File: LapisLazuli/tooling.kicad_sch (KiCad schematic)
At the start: 60 parts, among them J1 Conn_01x02, J10 Conn_01x03, J11 Conn_01x03, J12 Conn_01x02, J13 Conn_01x02, J2 Conn_01x02, J3 Conn_01x02, J4 Conn_01x02, J5 Conn_01x02, J6 Conn_01x02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

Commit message: Everything but I2C mux I think
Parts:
- added C44: 100n, symbol Device:C_Small
- added C45: 10u, symbol Device:C_Small
- added J14, J15: Conn_01x04, symbol Connector_Generic:Conn_01x04
- added J16: Conn_01x02, symbol Connector_Generic:Conn_01x02
- added R21: 120, symbol Device:R_Small_US
- added U13: LTC4311CSC6-TRPBF, SOT-6_SC_LIT, symbol 2025-11-21_17-52-57:LTC4311CSC6-TRPBF
- added U9: ISO1412DW, DW16_TEX, symbol 2025-11-15_19-07-41:ISO1412DW
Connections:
- net +5V: now also C44.2, C45.1, J14.4 (Pin_4), J15.4 (Pin_4), U13.1 (VCC), U13.3 (ENABLE), U9.1 (VCC1)
- net GND: now also C44.1, C45.2, J14.1 (Pin_1), J15.1 (Pin_1), U13.2 (GND), U13.5 (GND), U9.2 (GND1), U9.8 (GND1)
- net I2C_SCL: now also U13.4 (BUS2)
- net I2C_SDA: now also U13.6 (BUS1)
- new net ENCODER0_SCL: J14.2 (Pin_2)
- new net ENCODER0_SDA: J14.3 (Pin_3)
- new net ENCODER1_SCL: J15.2 (Pin_2)
- new net ENCODER1_SDA: J15.3 (Pin_3)
- new net GNDPWR: U9.15 (GND2), U9.9 (GND2)
- new net RS485_A: J16.2 (Pin_2), R21.1, U9.14 (A)
- new net RS485_B: J16.1 (Pin_1), R21.2, U9.13 (B)
- new net RS485_RX: U9.3 (R)
- new net RS485_SEND: U9.4 (*RE), U9.5 (DE)
- new net RS485_TX: U9.6 (D)
- no-connect marks 0 -> 2
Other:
- note added: "Encoder Headers"
- note added: "I2C Extender"
- note added: "RS485"
- note added: "idk what to do here"

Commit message: I2C Mux
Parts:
- added C46: 100n, symbol Device:C_Small
- added R22: 10k, symbol Device:R_Small_US
- added U14: TCA9546APWR, TCA9546APWR:SOP65P640X120-16N, symbol TCA9546APWR:TCA9546APWR
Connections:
- net +5V: now also C46.1, U14.16 (VCC)
- net ENCODER0_SCL: now also U14.5 (SC0)
- net ENCODER0_SDA: now also U14.4 (SD0)
- net ENCODER1_SCL: now also U14.7 (SC1)
- net ENCODER1_SDA: now also U14.6 (SD1)
- net GND: now also C46.2, U14.1 (A0), U14.13 (A2), U14.2 (A1), U14.8 (GND)
- net I2C_SCL: now also U14.15 (SDA)
- net I2C_SDA: now also U14.14 (SCL)
- new net I2C_MUX_RESET': R22.2, U14.3 (~{RESET})
- no-connect marks 2 -> 6
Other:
- note added: "I2C Mux"

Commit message: Most footprints and second I2C extender
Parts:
- added C47: 10u, Capacitor_SMD:C_0805_2012Metric, symbol Device:C_Small
- added U15: LTC4311CSC6-TRPBF, Package_TO_SOT_SMD:SOT-363_SC-70-6, symbol 2025-11-21_17-52-57:LTC4311CSC6-TRPBF
- C1, C10, C13, C14, C15, C16, C2, C35, C37, C39, C4, C41, C43, C44, C46, C5, C7, C8, C9: footprint (none) -> Capacitor_SMD:C_0603_1608Metric; Digikey (none) -> C14663; LCSC (none) -> C14663
- C11, C12, C3, C6: footprint (none) -> Capacitor_SMD:C_0805_2012Metric; Digikey (none) -> C16780; LCSC (none) -> C16780
- C36, C38, C40, C42: footprint (none) -> Capacitor_SMD:CP_Elec_6.3x7.7; Digikey (none) -> C3338; LCSC (none) -> C3338
- C45: footprint (none) -> Capacitor_SMD:C_0805_2012Metric; Digikey (none) -> C19702; LCSC (none) -> C19702
- J1, J12, J13, J16, J2, J3, J4, J5, J6: footprint (none) -> Connector_PinHeader_2.54mm:PinHeader_1x02_P2.54mm_Vertical
- J10, J11, J8, J9: footprint (none) -> Connector_PinHeader_2.54mm:PinHeader_1x03_P2.54mm_Vertical
- J14, J15: footprint (none) -> Connector_PinHeader_2.54mm:PinHeader_1x04_P2.54mm_Vertical
- J7: footprint (none) -> Connector_PinHeader_2.54mm:PinHeader_1x05_P2.54mm_Vertical
- MOSFET1, MOSFET2: footprint SOT-23_MCC -> Package_TO_SOT_SMD:SOT-23; LCSC (none) -> C10488
- R1, R10, R11, R12, R2, R22, R3, R4, R5, R6, R7, R8, R9: footprint (none) -> Resistor_SMD:R_0603_1608Metric; LCSC (none) -> C25804
- R21: footprint (none) -> Resistor_SMD:R_0603_1608Metric; LCSC (none) -> C22787
- U1, U3, U5, U6: LCSC (none) -> C5139865
- U13: footprint SOT-6_SC_LIT -> Package_TO_SOT_SMD:SOT-363_SC-70-6; LCSC (none) -> C580856
- U14: footprint TCA9546APWR:SOP65P640X120-16N -> Package_SO:TSSOP-16_4.4x5mm_P0.65mm; LCSC (none) -> C201653
- U2, U4, U7, U8: footprint SC70-6_2P2X1P35_ONS -> Package_TO_SOT_SMD:SOT-363_SC-70-6; LCSC (none) -> C462890
- U9: footprint DW16_TEX -> Package_SO:SOIC-16W_7.5x10.3mm_P1.27mm; LCSC (none) -> C2672327
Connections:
- net +5V: now also C47.1, U15.1 (VCC), U15.3 (ENABLE)
- net ENCODER0_SCL: now also U13.4 (BUS2)
- net ENCODER0_SDA: now also U13.6 (BUS1)
- net ENCODER1_SCL: now also U15.4 (BUS2)
- net ENCODER1_SDA: now also U15.6 (BUS1)
- net GND: now also C47.2, U15.2 (GND), U15.5 (GND)
- net I2C_SCL: no longer U13.4 (BUS2)
- net I2C_SDA: no longer U13.6 (BUS1)
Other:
- moved on the sheet: C44, C45, J16, R21, U13, U9

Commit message: Zaid Schematic Review
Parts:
- added C48, C51: 10u, Capacitor_SMD:C_0805_2012Metric, symbol Device:C_Small
- added C49, C50: 100n, Capacitor_SMD:C_0603_1608Metric, symbol Device:C_Small
- added D2, D3: BAT54SDW, Package_TO_SOT_SMD:SOT-363_SC-70-6, symbol Diode:BAT54SDW
- added T1: WE-PPTI_1512, WE-PPTI_1512:WE-PPTI_1512_L15.41W12.32H11.89, symbol WE-PPTI_1512:WE-PPTI_1512
- added U16: SN6505BDBVT, DBV0006A_N, symbol 2025-12-09_17-00-03:SN6505BDBVT
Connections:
- net +5V: now also C48.1, T1.2, U16.2 (VCC), U16.5 (EN)
- net GND: now also C48.2, U16.4 (GND), U16.6 (CLK)
- net GNDPWR: now also C49.2, C50.2, C51.2, D3.6 (K), T1.5
- net I2C_SCL: now also U14.14 (SCL); no longer U14.15 (SDA)
- net I2C_SDA: now also U14.15 (SDA); no longer U14.14 (SCL)
- net RS485_A: now also U9.11 (Y)
- net RS485_B: now also U9.12 (Z)
- net +5VA: now reaches U9.16 (VCC2)
- net +5VA: now also C49.1, C50.1, C51.1, D2.6 (K)
- new net: T1.1, U16.1 (D1)
- new net: T1.3, U16.3 (D2)
- new net: D3.1 (A), T1.4
- new net: D2.1 (A), T1.6
- no-connect marks 6 -> 4
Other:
- note removed: "idk what to do here"
- moved on the sheet: J16

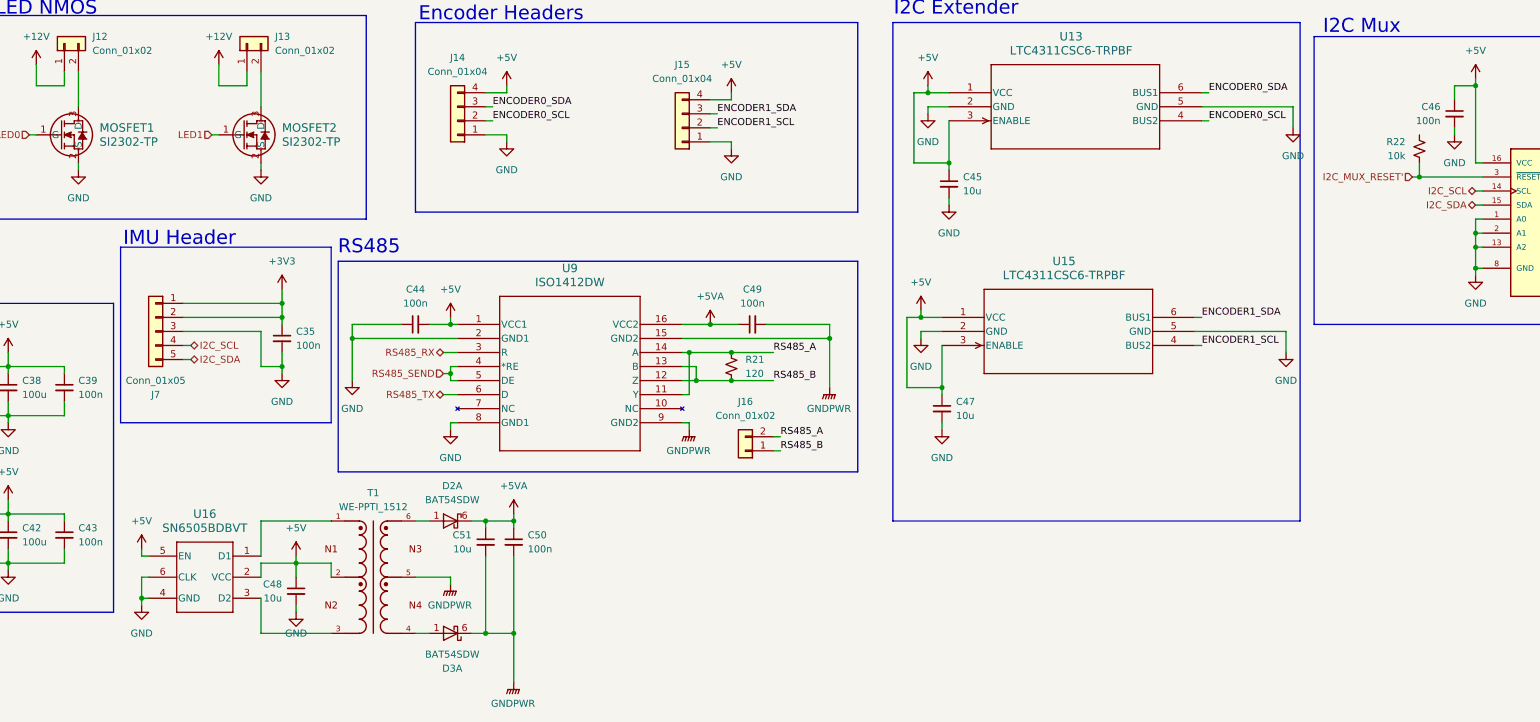
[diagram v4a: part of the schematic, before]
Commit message: Add current pcb layout
- Missing connections to power board
- Missing LEDs
- Missing Test Points
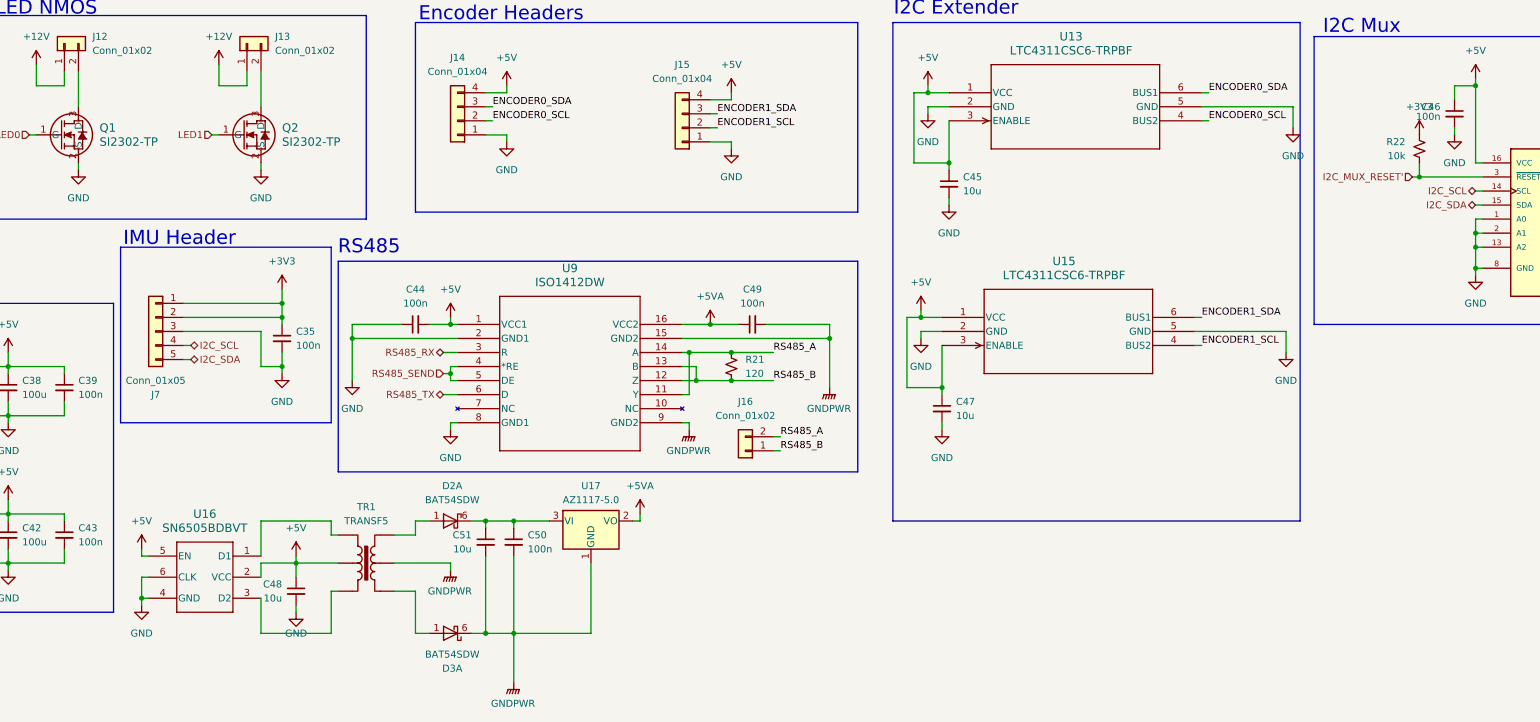
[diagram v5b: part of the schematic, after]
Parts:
- removed T1: WE-PPTI_1512, WE-PPTI_1512:WE-PPTI_1512_L15.41W12.32H11.89, symbol WE-PPTI_1512:WE-PPTI_1512
- added TR1: TRANSF5, footprints:WE-PPTI_1006_L10.2W6.73H4.19, symbol Transformer:TRANSF5
- added U17: AZ1117-5.0, Package_TO_SOT_SMD:SOT-223-3_TabPin2, symbol Regulator_Linear:AZ1117-5.0
- U16: footprint DBV0006A_N -> Package_TO_SOT_SMD:SOT-23-6
- renumbered MOSFET1 to Q1, MOSFET2 to Q2
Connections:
- net +3V3: now also R22.1
- net +5V: now also TR1.2
- net +5VA: now also U17.2 (VO); no longer C50.1, C51.1, D2.6 (K)
- net GNDPWR: now also TR1.5, U17.1 (GND)
- net at U16.1 (D1): now also TR1.1
- net at U16.3 (D2): now also TR1.3
- net at D3.1 (A): now also TR1.4
- net at D2.1 (A): now also TR1.6
- new net: C50.1, C51.1, D2.6 (K), U17.3 (VI)
